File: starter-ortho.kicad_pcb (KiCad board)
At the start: 2 copper layers, 98 parts, among them SW1 SW_Push, U1 ProMicro

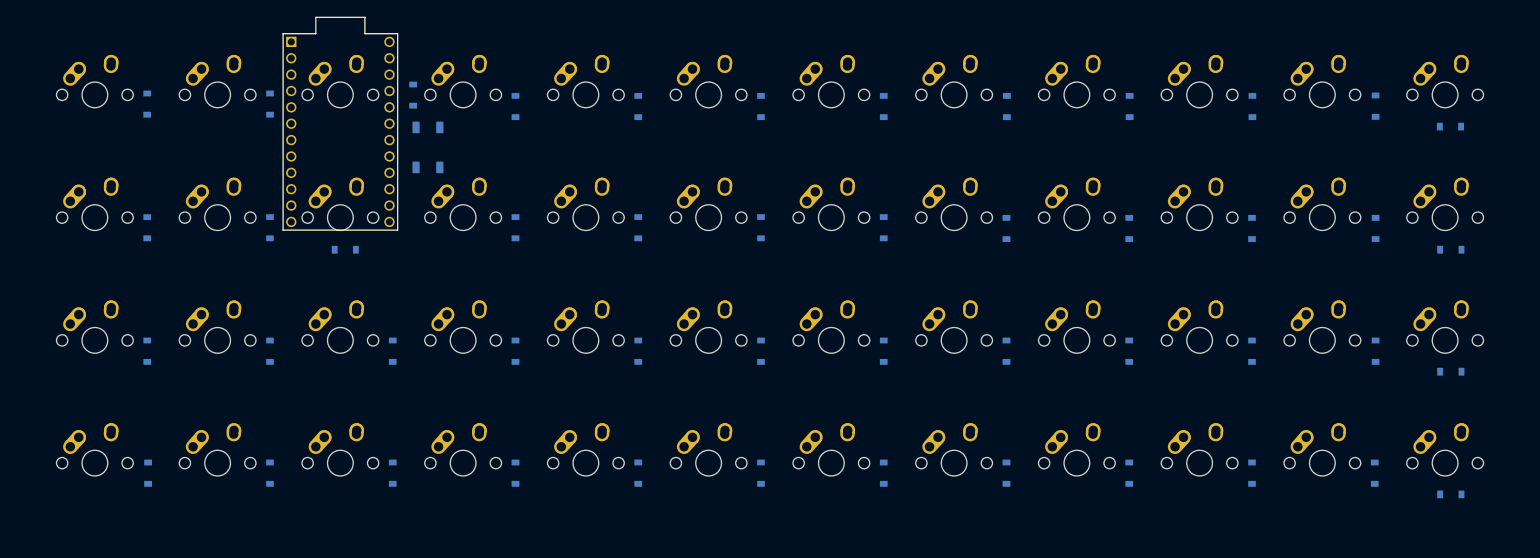
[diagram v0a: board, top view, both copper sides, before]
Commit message: Added edges and M2 holes
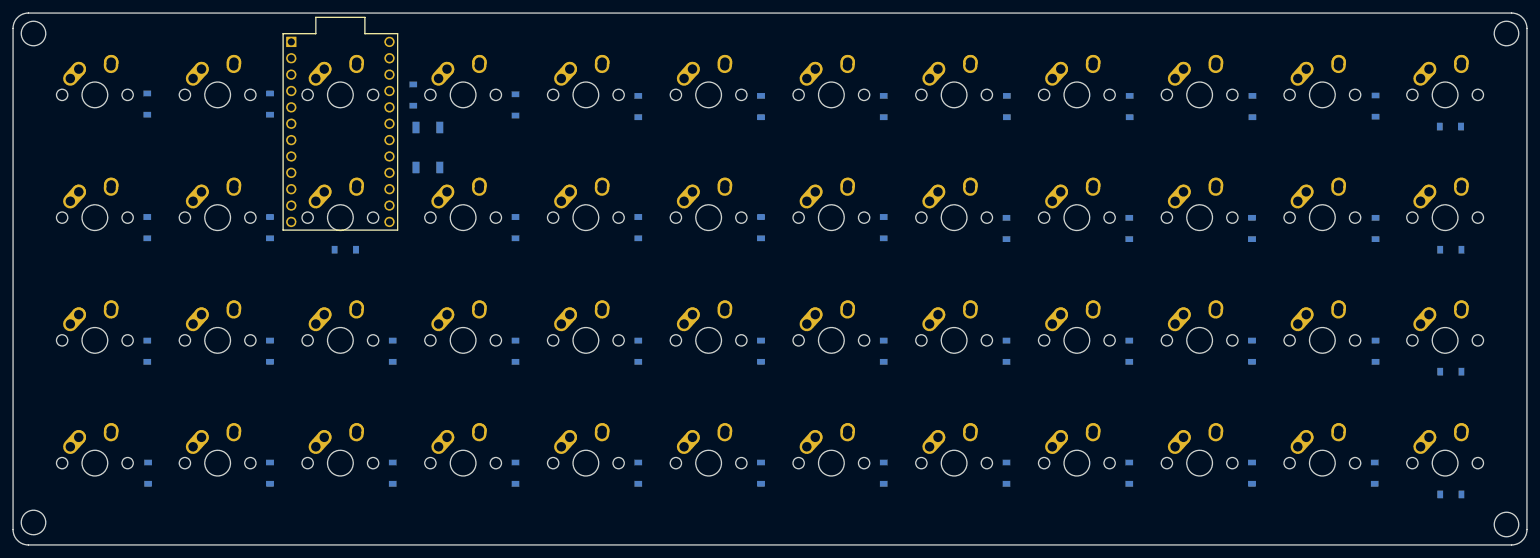
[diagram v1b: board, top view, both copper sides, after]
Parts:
- moved D13 0.25 mm to (125.6, 29.3)
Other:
- board outline added: 235 x 82.5 mm
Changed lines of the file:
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@@
   (general
     (thickness 1.6)
-    (drawings 0)
+    (drawings 12)
     (tracks 0)
     (zones 0)
@@
   )
   (module Diode_SMD:D_SOD-123 (layer B.Cu)
-    (at 125.603 29.591 90)
+    (at 125.603 29.337 90)
     (descr SOD-123)
     (tags SOD-123)
@@
     )
   )
+  (gr_circle (center 50.8 94.14375) (end 52.7 94.14375) (layer Edge.Cuts) (width 0.05))
+  (gr_circle (center 50.8 18.25625) (end 52.7 18.25625) (layer Edge.Cuts) (width 0.05))
+  (gr_circle (center 279.4 18.25625) (end 281.3 18.25625) (layer Edge.Cuts) (width 0.05))
+  (gr_circle (center 279.4 94.45625) (end 281.3 94.45625) (layer Edge.Cuts) (width 0.05))
+  (gr_line (start 280.19375 15.08125) (end 50.00625 15.08125) (layer Edge.Cuts) (width 0.05))
+  (gr_line (start 282.575 95.25) (end 282.575 17.4625) (layer Edge.Cuts) (width 0.05))
+  (gr_line (start 50.00625 97.63125) (end 280.19375 97.63125) (layer Edge.Cuts) (width 0.05))
+  (gr_line (start 47.625 17.4625) (end 47.625 95.25) (layer Edge.Cuts) (width 0.05))
+  (gr_arc (start 50.00625 17.4625) (end 50.00625 15.08125) (angle -90) (layer Edge.Cuts) (width 0.05))
+  (gr_arc (start 50.00625 95.25) (end 47.625 95.25) (angle -90) (layer Edge.Cuts) (width 0.05))
+  (gr_arc (start 280.19375 95.25) (end 280.19375 97.63125) (angle -90) (layer Edge.Cuts) (width 0.05))
+  (gr_arc (start 280.19375 17.4625) (end 282.575 17.4625) (angle -90) (layer Edge.Cuts) (width 0.05))
 )

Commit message: Routed traces (poorly)
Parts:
- U1: moved to B.Cu
- moved SW1 75.7 mm to (37.3, 23.8), turned to 180 degrees
- moved U1 61.1 mm to (37.3, 33.5)
- moved D10 8.13 mm to (106.6, 48.4), turned to 90 degrees
- moved D9 3.52 mm to (106.6, 29.3)
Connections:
- U1 pad 17: COL3 -> COL0
- U1 pad 18: COL2 -> COL1
- U1 pad 19: COL1 -> COL2
- U1 pad 20: COL0 -> COL3
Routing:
- net COL11: track 0.00 -> 358.2 mm
- net COL10: track 0.00 -> 332.6 mm
- net COL9: track 0.00 -> 310.0 mm
- net COL8: track 0.00 -> 286.2 mm
- net ROW3: track 0.00 -> 279.0 mm
- net COL7: track 0.00 -> 270.1 mm
- net ROW0: track 0.00 -> 264.8 mm
- net ROW2: track 0.00 -> 264.8 mm
- net COL6: track 0.00 -> 241.3 mm
- net ROW1: track 0.00 -> 224.8 mm
- net COL5: track 0.00 -> 216.7 mm
- net COL4: track 0.00 -> 193.6 mm
- net COL3: track 0.00 -> 156.0 mm
- net COL2: track 0.00 -> 138.0 mm
- net COL1: track 0.00 -> 119.9 mm
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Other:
- board size 235 x 82.5 mm -> 258.8 x 82.5 mm
- net class Default: trace_width 0.25 -> 0.254
- net class Power added: clearance 0.2, trace_width 0.381, via_dia 0.8, via_drill 0.4

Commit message: undid edge cuts
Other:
- board size 258.8 x 82.5 mm -> 2.4 x 2.4 mm
- board text added: "starter-ortho Reid Schneyer Dec 2019"

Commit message: we're doing choc switches now baby
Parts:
- SW1: moved to F.Cu
- moved SW1 121.3 mm to (149.2, 70.6)
- moved U1 111.7 mm to (147.6, 50.8)
- moved D1 40.5 mm to (31.9, 46.7)
- moved D10 40.5 mm to (70.0, 65.8)
- moved D11 40.5 mm to (70.0, 85.0)
- moved D12 40.5 mm to (70.0, 103.9)
- moved D2 40.5 mm to (31.9, 65.8)
- moved D21 40.5 mm to (127.2, 47.1)
- moved D22 40.5 mm to (127.2, 65.8)
- moved D23 40.5 mm to (127.2, 85.0)
- moved D24 40.5 mm to (127.2, 103.9)
- moved D3 40.5 mm to (31.9, 85.0)
- moved D5 40.5 mm to (51.0, 46.7)
- moved D6 40.5 mm to (51.0, 65.8)
- moved D7 40.5 mm to (51.0, 85.0)
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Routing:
- net COL11: track 358.2 -> 0.00 mm
- net COL10: track 332.6 -> 0.00 mm
- net COL9: track 310.0 -> 0.00 mm
- net COL8: track 286.2 -> 0.00 mm
- net ROW3: track 279.0 -> 0.00 mm
- net COL7: track 270.1 -> 0.00 mm
- net ROW0: track 264.8 -> 0.00 mm
- net ROW2: track 264.8 -> 0.00 mm
- net COL6: track 241.3 -> 0.00 mm
- net ROW1: track 224.8 -> 0.00 mm
- net COL5: track 216.7 -> 0.00 mm
- net COL4: track 193.6 -> 0.00 mm
- net COL3: track 156.0 -> 0.00 mm
- net COL2: track 138.0 -> 0.00 mm
- net COL1: track 119.9 -> 0.00 mm
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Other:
- board outline removed
- board text removed: "starter-ortho Reid Schneyer Dec 2019"

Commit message: all traces routed
done well? we'll see...
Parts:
- MX1, MX10, MX11, MX12, MX13, MX14, MX15, MX16, MX17, MX18, MX19, MX2, MX20, MX21, MX22, MX23, MX24, MX25, MX26, MX27, MX28, MX29, MX3, MX30, MX31, MX32, MX33, MX34, MX35, MX36, MX37, MX38, MX39, MX4, MX40, MX41, MX42, MX43, MX44, MX45, MX46, MX47, MX48, MX5, MX6, MX7, MX8, MX9: footprint MX_Alps_Hybrid:MX-1U-NoLED -> Kailh_Choc:KailhChoc-1U
- moved D48 7.99 mm to (279.7, 104.0), turned to 90 degrees
- moved D45 7.90 mm to (279.5, 47.0), turned to 90 degrees
- moved D46 7.87 mm to (279.5, 66.0), turned to 90 degrees
- moved D47 7.82 mm to (279.5, 85.1), turned to 90 degrees
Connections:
- U1 pad 1: Net-(U1-Pad1) -> COL11
- U1 pad 10: COL6 -> Net-(U1-Pad10)
- U1 pad 11: COL5 -> ROW0
- U1 pad 12: COL4 -> ROW1
- U1 pad 15: ROW1 -> COL5
- U1 pad 16: ROW0 -> COL4
- U1 pad 17: COL0 -> COL3
- U1 pad 18: COL1 -> COL2
- U1 pad 19: COL2 -> COL1
- U1 pad 2: Net-(U1-Pad2) -> COL10
- U1 pad 20: COL3 -> COL0
- U1 pad 5: COL11 -> COL9
- U1 pad 6: COL10 -> COL8
- U1 pad 7: COL9 -> COL7
- U1 pad 8: COL8 -> COL6
- U1 pad 9: COL7 -> Net-(U1-Pad9)
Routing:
- net ROW3: track 0.00 -> 294.3 mm
- net ROW2: track 0.00 -> 281.4 mm
- net ROW0: track 0.00 -> 272.8 mm
- net ROW1: track 0.00 -> 254.0 mm
- net COL11: track 0.00 -> 184.4 mm
- net COL0: track 0.00 -> 177.8 mm
- net COL10: track 0.00 -> 165.4 mm
- net COL1: track 0.00 -> 160.5 mm
- net COL2: track 0.00 -> 149.6 mm
- net COL9: track 0.00 -> 148.3 mm
- net COL3: track 0.00 -> 129.5 mm
- net COL8: track 0.00 -> 128.2 mm
- net COL4: track 0.00 -> 110.7 mm
- net COL7: track 0.00 -> 108.1 mm
- net COL5: track 0.00 -> 92.3 mm
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
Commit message: PCB done?
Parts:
- moved D10 20.1 mm to (71.4, 45.8)
- moved D2 20.1 mm to (33.3, 45.8)
- moved D22 20.1 mm to (128.6, 45.8)
- moved D26 20.1 mm to (185.7, 45.8)
- moved D6 20.1 mm to (52.4, 45.8)
- moved D1 20.1 mm to (33.3, 26.6)
- moved D11 20.1 mm to (71.4, 65.0)
- moved D12 20.1 mm to (71.4, 83.9)
- moved D14 20.1 mm to (90.5, 45.8)
- moved D18 20.1 mm to (109.5, 45.8)
- moved D21 20.1 mm to (128.6, 27.0)
- moved D23 20.1 mm to (128.6, 65.0)
- moved D24 20.1 mm to (128.6, 83.9)
- moved D25 20.1 mm to (185.7, 27.0)
- moved D27 20.1 mm to (185.7, 65.0)
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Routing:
- net GND: track 48.8 -> 50.5 mm
- net Net-(SW1-Pad1): track 29.4 -> 28.7 mm
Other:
- board outline added: 272.3 x 82.6 mm
- board text added: "Reid Schneyer Splitish Ortho"

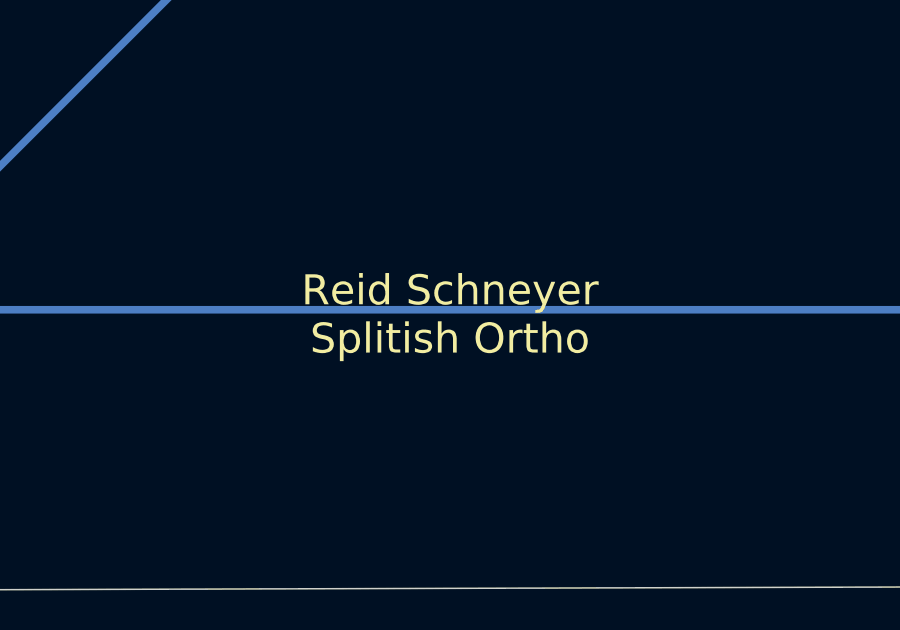
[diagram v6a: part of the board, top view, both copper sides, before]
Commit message: removed name from silkscreen
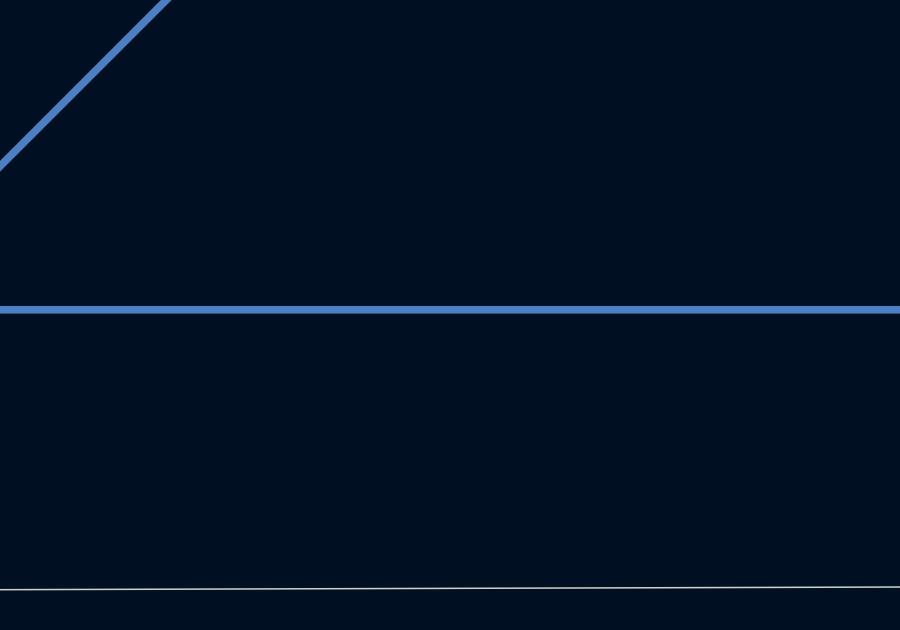
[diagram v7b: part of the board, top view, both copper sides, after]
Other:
- board text removed: "Reid Schneyer Splitish Ortho"
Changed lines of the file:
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@@
   (general
     (thickness 1.6)
-    (drawings 10)
+    (drawings 9)
     (tracks 515)
     (zones 0)
@@
     )
   )
-  (gr_text "Reid Schneyer\nSplitish Ortho" (at 149.225 85.725) (layer F.SilkS)
-    (effects (font (size 1 1) (thickness 0.15)))
-  )
   (gr_line (start 282.575 94.45625) (end 15.08125 95.25) (layer Edge.Cuts) (width 0.05))

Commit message: generated gerber files
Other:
- board text added: "Split-ish Ortho"
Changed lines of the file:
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@@
   (general
     (thickness 1.6)
-    (drawings 9)
+    (drawings 10)
     (tracks 515)
     (zones 0)
@@
     )
   )
+  (gr_text "Split-ish Ortho" (at 149.225 88.9) (layer F.SilkS)
+    (effects (font (size 5 3) (thickness 0.15)))
+  )
   (gr_line (start 282.575 94.45625) (end 15.08125 95.25) (layer Edge.Cuts) (width 0.05))
